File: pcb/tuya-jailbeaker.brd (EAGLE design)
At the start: 19.5 x 15 mm, 17 parts, among them U1 ESP8285, X1 26MHz

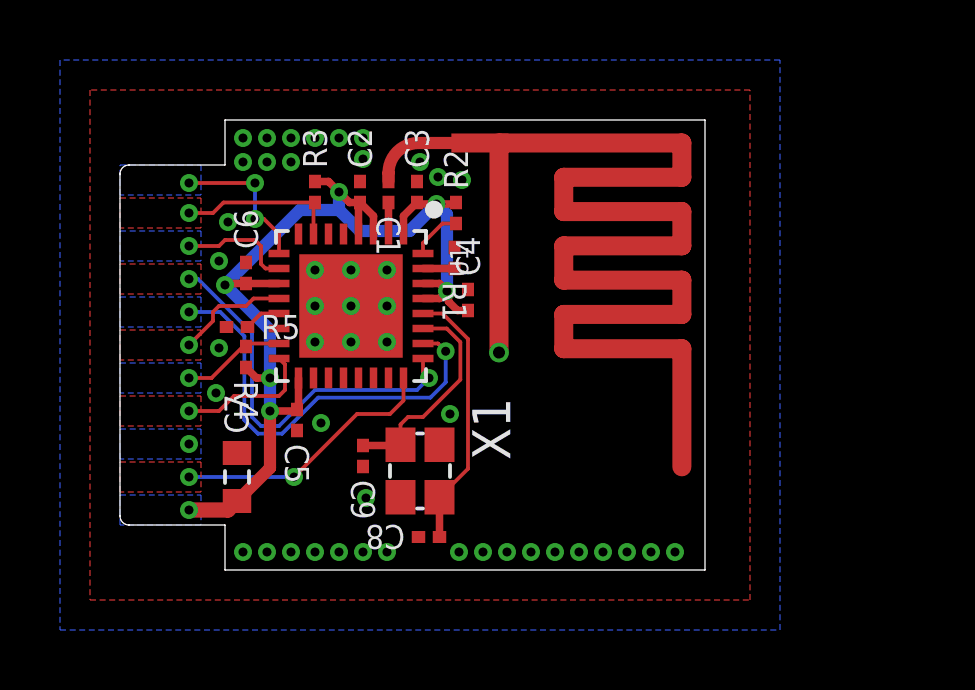
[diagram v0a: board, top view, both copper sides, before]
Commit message: Add logo Generate schematic PDF
Signed-off-by: João Silva <jgc3silva@gmail.com>
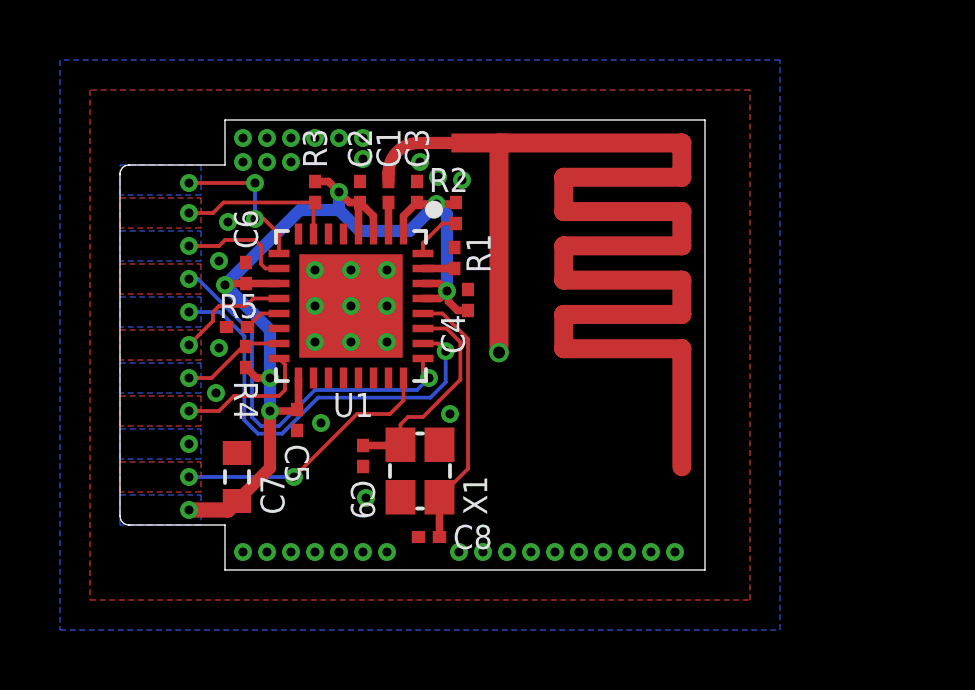
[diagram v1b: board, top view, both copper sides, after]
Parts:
- added LOGO1: JS-5MM, Silkscreen:JS_5MM
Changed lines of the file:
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@@
 <wire x1="0" y1="13.2" x2="0.3" y2="13.5" width="0" layer="20" curve="-90"/>
 <wire x1="0.3" y1="13.5" x2="3.5" y2="13.5" width="0" layer="20"/>
-<text x="11.5" y="1.5" size="0.8" layer="22" font="vector" ratio="10" rot="MR0" align="center">Tuya Jailbreaker v1
+<text x="11.5" y="2.1" size="0.8" layer="22" font="vector" ratio="10" rot="MR0" align="center">Tuya Jailbreaker v1
 Jun 2021</text>
 <wire x1="3.5" y1="13.5" x2="3.5" y2="15" width="0" layer="20"/>
@@
 <element name="E1" library="Antenna" package="OLIMEX_ANT_ESP8266_ANT" value="2.4GHZ" x="15.3" y="8.9" smashed="yes" rot="R270"/>
 <element name="U1" library="Espressif" package="QFN32" value="ESP8285" x="7.7" y="8.8" smashed="yes" rot="R270">
-<attribute name="NAME" x="11" y="10.8" size="0.6096" layer="25" rot="R270"/>
+<attribute name="NAME" x="7.1" y="5.5" size="0.8" layer="25" font="vector" ratio="10" align="center-left"/>
 </element>
 <element name="C1" library="Capacitor" package="CAP0201" value="5.6pF" x="8.95" y="12.6" smashed="yes" rot="R270">
-<attribute name="NAME" x="8.95" y="11.800003125" size="0.8" layer="25" font="vector" ratio="10" rot="SR270" align="center-left"/>
+<attribute name="NAME" x="8.95" y="13.4" size="0.8" layer="25" font="vector" ratio="10" rot="SR90" align="center-left"/>
 <attribute name="VOLTAGE" value="" x="8.95" y="12.6" size="1.778" layer="27" rot="R270" display="off"/>
 </element>
 <element name="R1" library="Resistor" package="RES0201" value="12K Ohms" x="11.15" y="10.4" smashed="yes" rot="R270">
-<attribute name="NAME" x="11.15" y="9.6" size="0.8" layer="25" font="vector" ratio="10" rot="SR270" align="center-left"/>
+<attribute name="NAME" x="11.95" y="9.9" size="0.8" layer="25" font="vector" ratio="10" rot="SR90" align="center-left"/>
 <attribute name="POWER" value="" x="11.15" y="10.4" size="1.778" layer="27" rot="R270" display="off"/>
 <attribute name="TOLERANCE" value="" x="11.15" y="10.4" size="1.778" layer="27" rot="R270" display="off"/>
@@
 </element>
 <element name="C4" library="Capacitor" package="CAP0201" value="100nF" x="11.6" y="9" smashed="yes" rot="R90">
-<attribute name="NAME" x="11.6" y="9.8" size="0.8" layer="25" font="vector" ratio="10" rot="SR90" align="center-left"/>
+<attribute name="NAME" x="11.1" y="7.2" size="0.8" layer="25" font="vector" ratio="10" rot="SR90" align="center-left"/>
 <attribute name="VOLTAGE" value="" x="11.3" y="8.6" size="1.778" layer="27" rot="R90" display="off"/>
 </element>
@@
 </element>
 <element name="C7" library="Capacitor" package="CAP0603" value="10uF" x="3.9" y="3.1" smashed="yes" rot="R90">
-<attribute name="NAME" x="3.884" y="4.5456" size="0.8" layer="25" font="vector" ratio="10" rot="SR90" align="center-left"/>
+<attribute name="NAME" x="5.084" y="1.8456" size="0.8" layer="25" font="vector" ratio="10" rot="SR90" align="center-left"/>
 <attribute name="VOLTAGE" value="" x="3.9" y="3.1" size="1.778" layer="27" rot="R90" display="off"/>
 </element>
 <element name="R2" library="Resistor" package="RES0201" value="10K Ohms" x="11.2" y="11.9" smashed="yes" rot="R90">
-<attribute name="NAME" x="11.2" y="12.7" size="0.8" layer="25" font="vector" ratio="10" rot="SR90" align="center-left"/>
+<attribute name="NAME" x="10.3" y="13" size="0.8" layer="25" font="vector" ratio="10" rot="SR0" align="center-left"/>
 <attribute name="POWER" value="" x="10.9" y="11.5" size="1.778" layer="27" rot="R90" display="off"/>
 <attribute name="TOLERANCE" value="" x="10.9" y="11.5" size="1.778" layer="27" rot="R90" display="off"/>
@@
 </element>
 <element name="X1" library="Crystal" package="4-SMD-2520" value="26MHz" x="10" y="3.3" smashed="yes" rot="R270">
-<attribute name="NAME" x="11.74" y="5.74" size="1.27" layer="25" rot="R270"/>
+<attribute name="NAME" x="11.84" y="3.14" size="0.8" layer="25" font="vector" ratio="10" rot="R270" align="center-left"/>
+<attribute name="OCLCSC" value="C709005" x="10" y="3.3" size="1.778" layer="27" rot="R270" display="off"/>
 </element>
 <element name="C8" library="Capacitor" package="CAP0201" value="9pF" x="10.3" y="1.1" smashed="yes" rot="R180">
-<attribute name="NAME" x="9.5" y="1.1" size="0.8" layer="25" font="vector" ratio="10" rot="SR180" align="center-left"/>
+<attribute name="NAME" x="11.1" y="1.1" size="0.8" layer="25" font="vector" ratio="10" rot="SR0" align="center-left"/>
 <attribute name="VOLTAGE" value="" x="10.7" y="0.8" size="1.778" layer="27" rot="R180" display="off"/>
 </element>
@@
 </element>
 <element name="R5" library="Resistor" package="RES0201" value="10K Ohms" x="3.9" y="8.1" smashed="yes">
-<attribute name="NAME" x="4.7" y="8.1" size="0.8" layer="25" font="vector" ratio="10" rot="SR0" align="center-left"/>
+<attribute name="NAME" x="3.3" y="8.8" size="0.8" layer="25" font="vector" ratio="10" rot="SR0" align="center-left"/>
 <attribute name="POWER" value="" x="3.5" y="8.4" size="1.778" layer="27" display="off"/>
 <attribute name="TOLERANCE" value="" x="3.5" y="8.4" size="1.778" layer="27" display="off"/>
 </element>
+<element name="LOGO1" library="Silkscreen" package="JS_5MM" value="JS-5MM" x="13.3" y="11.3" smashed="yes" rot="MR0"/>
 </elements>
 <signals>

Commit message: Update to ESP32-C3
Signed-off-by: João Silva <jgc3silva@gmail.com>
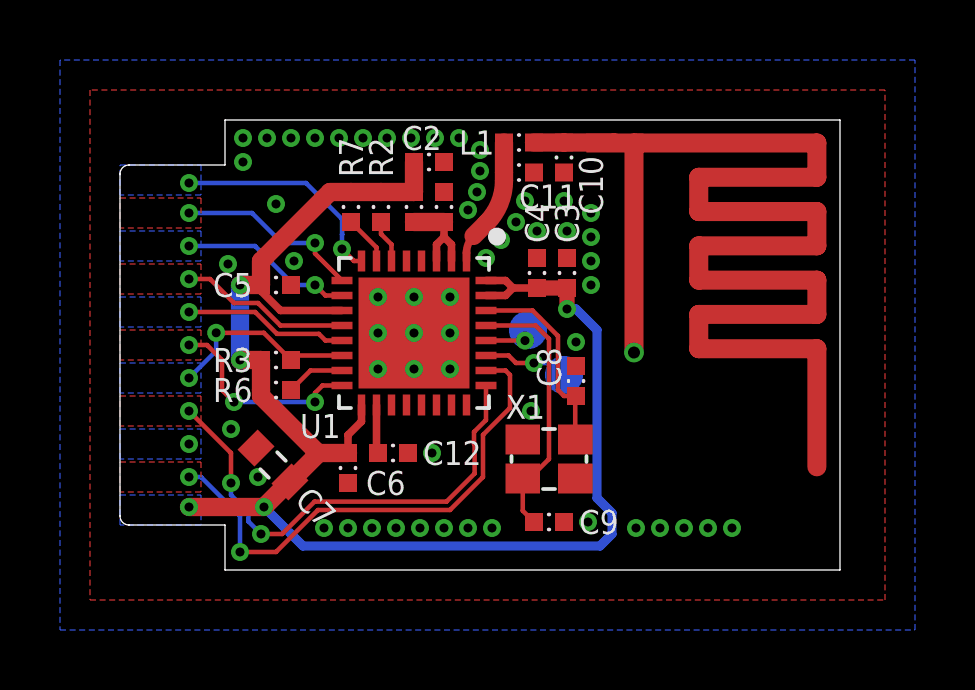
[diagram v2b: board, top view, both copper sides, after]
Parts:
- removed R1: 12K Ohms, Resistor:RES0201
- removed R4, R5: 10K Ohms, Resistor:RES0201
- added C10, C11: TBD, Capacitor:CAP0402
- added C12: 1uF, Capacitor:CAP0402
- added L1: TBD, Inductor:IND0402
- added L2: 2nH, Inductor:IND0402
- added R6, R7: 1K Ohms, Resistor:RES0402
- added TP1, TP2: TESTPOINT-1.27MM, PADs:PAD1.27MM
- C1: value 5.6pF -> 1uF; device Capacitor:CAP0201 -> Capacitor:CAP0402
- C2, C5, C6, C8, C9: device Capacitor:CAP0201 -> Capacitor:CAP0402
- C3: value 100nF -> 1uF; device Capacitor:CAP0201 -> Capacitor:CAP0402
- C4: value 100nF -> 10nF; device Capacitor:CAP0201 -> Capacitor:CAP0402
- R2, R3: value 10K Ohms -> 1K Ohms; device Resistor:RES0201 -> Resistor:RES0402
- U1: value ESP8285 -> ESP32-C3FH4
- X1: value 26MHz -> 40MHz
- moved C6 7.34 mm to (7.60, 3.40), turned to 270 degrees
- moved C8 7.14 mm to (15.2, 6.30), turned to 90 degrees
- moved C9 6.58 mm to (14.3, 1.60), turned to 0 degrees
- moved R3 5.75 mm to (5.20, 7.00), turned to 180 degrees
- moved C3 5.68 mm to (14.9, 9.90)
- moved LOGO1 5.01 mm to (18.3, 11.0)
- moved C5 4.55 mm to (5.20, 9.50), turned to 0 degrees
- moved E1 4.50 mm to (19.8, 8.90)
- moved X1 4.32 mm to (14.3, 3.70), turned to 0 degrees
- moved C2 2.51 mm to (10.3, 13.6), turned to 0 degrees
- moved R2 2.51 mm to (8.70, 12.1)
- moved C4 2.47 mm to (13.9, 9.90)
- moved U1 2.28 mm to (9.80, 7.90)
- moved C1 1.92 mm to (10.8, 12.1), turned to 90 degrees
- moved C7 1.26 mm to (5.10, 3.50), turned to 135 degrees
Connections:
- net !BLUE_LED renamed GPIO6
- net BL0937_CF renamed GPIO10
- net BL0937_SEL renamed GPIO5
- net RELAY_RED_LED renamed GPIO4
- removed net !BTN: R4.1, U1.15
- removed net BL0937_CF1: U1.24
- removed net N$1: C1.2, U1.2
- removed net N$2: C1.1, E1.ANT
- removed net N$3: R1.2, U1.31
- removed net N$4: R2.1, U1.32
- removed net N$5: C8.1, U1.28, X1.3
- removed net N$6: C9.1, U1.27, X1.1
- removed net N$7: R5.2, U1.13
- new net ANT: C10.1, E1.ANT, L1.2
- new net GPIO18: U1.25
- new net GPIO19: U1.26
- new net GPIO2: R2.1, U1.6
- new net GPIO3: U1.8
- new net GPIO7: U1.13
- new net GPIO8: R3.1, U1.14
- new net GPIO9: R6.1, U1.15
- new net LNA_IN: C11.1, L1.1, U1.1
- new net VDD_LNA: C1.1, L2.2, U1.2, U1.3
- new net VDD_SPI: C12.1, U1.18
- new net XTALN: C9.1, U1.29, X1.1
- new net XTALP: C8.1, U1.30, X1.3
- net 3V3: now also L2.1, R6.2, R7.2, U1.31, U1.32; no longer R4.2, U1.1, U1.29, U1.3, U1.30, U1.4
- net CEN: now also R7.1; no longer R3.1
- net FLASH_RX: now also TP1.TP, U1.27; no longer U1.25
- net FLASH_TX: now also TP2.TP, U1.28; no longer U1.26
- net GND: now also C1.2, C10.2, C11.2, C12.2; no longer R1.1, R5.1
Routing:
- net GPIO19: track 0.00 -> 17.2 mm, vias 0 -> 2
- net GPIO18: track 0.00 -> 16.2 mm, vias 0 -> 3
- net 3V3: track 36.8 -> 51.8 mm, vias 7 -> 5
- net FLASH_TX: track 14.5 -> 1.70 mm, vias 2 -> 1
- net FLASH_RX: track 13.1 -> 2.87 mm, vias 2 -> 1
- net XTALN: track 0.00 -> 9.04 mm
- net BL0937_CF1: track 8.96 -> 0.00 mm, vias 2 -> 0
- net N$5: track 8.85 -> 0.00 mm
- net GPIO3: track 0.00 -> 7.42 mm, vias 0 -> 2
- net N$6: track 7.23 -> 0.00 mm
- net XTALP: track 0.00 -> 6.70 mm
- net GPIO8: track 0.00 -> 6.51 mm, vias 0 -> 2
- net GPIO7: track 0.00 -> 5.49 mm, vias 0 -> 1
- net LNA_IN: track 0.00 -> 4.29 mm
- net CEN: track 5.42 -> 1.65 mm, vias 1 -> 0
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- added copper zone on layer 1, net GPIO18
- added copper zone on layer 1, net GPIO19
- added copper zone on layer 16, net GPIO3
- added copper zone on layer 1, net GPIO4
- added copper zone on layer 16, net GPIO7
- added copper zone on layer 16, net GPIO8
- removed copper zone on layer 16, net !BTN
- removed copper zone on layer 1, net BL0937_CF1
- removed copper zone on layer 1, net CEN
- removed copper zone on layer 1, net FLASH_RX
- removed copper zone on layer 16, net FLASH_TX
- removed copper zone on layer 16, net GPIO4
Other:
- board size 19.5 x 15 mm -> 24 x 15 mm
- board text added: "Tuya Jailbreaker v2 Sep 2024"
- board text removed: "Tuya Jailbreaker v1 Jun 2021"
